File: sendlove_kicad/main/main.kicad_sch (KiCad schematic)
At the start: 0 parts

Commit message: feat(hw): schematic khoi nguon (USB-C, ESD, sac TP4056 + NTC, power-path, LDO)
- USB-C 16P, CC1/CC2 moi chan 5.1k rieng xuong GND, USBLC6-2SC6 tren D+/D-.
- TP4056: PROG 2k (~580mA), TEMP = NTC 10k B3950 + 6.2k tu VBUS (cua so sac
  ~5-45 do C, tinh theo nguong 45%/80% VCC; can doi chieu datasheet TP4056-42),
  CHRG -> LED do + 1k, STDBY bo trong.
- Power-path: VBUS -> SS14 -> VPATH; VBAT -> AO3401A (D=VBAT, S=VPATH,
  G=VBUS, 100k keo G xuong GND). Cong tac truot VPATH -> VSYS (sac van chay
  khi tat may).
- RT9080-33 (EN noi VSYS), 10uF vao/ra.
Them so voi BOM.md: NTC + 6.2k, 100k keo cong P-MOS, 10uF VBUS/VBAT.
Toan bo net noi bang nhan cuc bo; PWR_FLAG cho GND/VBUS/VSYS. ERC 0 loi.

Co-Authored-By: Claude Opus 5.5 <noreply@anthropic.com>
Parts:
- added C1, C2, C3, C4: 10uF, Capacitor_SMD:C_0805_2012Metric, symbol Device:C
- added D1: SS14, Diode_SMD:D_SMA, symbol Device:D_Schottky
- added D2: LED_Red, LED_SMD:LED_0603_1608Metric, symbol Device:LED
- added J1: USB-C 16P, Connector_USB:USB_C_Receptacle_HRO_TYPE-C-31-M-12, symbol Connector:USB_C_Receptacle_USB2.0_16P
- added J2: BATT, Connector_JST:JST_PH_S2B-PH-SM4-TB_1x02-1MP_P2.00mm_Horizontal, symbol Connector_Generic:Conn_01x02
- added Q1: AO3401A, Package_TO_SOT_SMD:SOT-23, symbol Transistor_FET:AO3401A
- added R1, R2: 5.1k, Resistor_SMD:R_0603_1608Metric, symbol Device:R
- added R3: 2k, Resistor_SMD:R_0603_1608Metric, symbol Device:R
- added R4: 6.2k 1%, Resistor_SMD:R_0603_1608Metric, symbol Device:R
- added R5: 1k, Resistor_SMD:R_0603_1608Metric, symbol Device:R
- added R6: 100k, Resistor_SMD:R_0603_1608Metric, symbol Device:R
- added SW1: POWER, Button_Switch_SMD:SW_SPDT_PCM12, symbol Switch:SW_SPDT
- added TH1: 10k B3950, Resistor_SMD:R_0603_1608Metric, symbol Device:Thermistor_NTC
- added U1: USBLC6-2SC6, Package_TO_SOT_SMD:SOT-23-6, symbol Power_Protection:USBLC6-2SC6
- added U2: TP4056-42-ESOP8, Package_SO:SOIC-8-1EP_3.9x4.9mm_P1.27mm_EP2.41x3.3mm_ThermalVias, symbol Battery_Management:TP4056-42-ESOP8
- added U3: RT9080-33GJ5, Package_TO_SOT_SMD:SOT-23-5, symbol SendLove:RT9080-33GJ5
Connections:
- new net +3V3: C4.1, U3.5 (VOUT)
- new net BAT_NTC: R4.2, TH1.1, U2.1 (TEMP)
- new net CC1: J1.A5 (CC1), R1.1
- new net CC2: J1.B5 (CC2), R2.1
- new net CHG_LED_K: D2.1 (K), R5.1
- new net CHG_PROG: R3.1, U2.2 (PROG)
- new net CHG_STAT: R5.2, U2.7 (~{CHRG})
- new net GND: C1.2, C2.2, C3.2, C4.2, J1.A1 (GND), J1.A12 (GND), J1.B1 (GND), J1.B12 (GND), J1.SH (SHIELD), J2.2 (Pin_2), R1.2, R2.2, R3.2, R6.2, TH1.2, U1.2 (GND), U2.3 (GND), U2.9 (EPAD), U3.2 (GND)
- new net USB_DN: J1.A7 (D-), J1.B7 (D-), U1.1 (I/O1), U1.6 (I/O1)
- new net USB_DP: J1.A6 (D+), J1.B6 (D+), U1.3 (I/O2), U1.4 (I/O2)
- new net VBAT: C2.1, J2.1 (Pin_1), Q1.3 (D), U2.5 (BAT)
- new net VBUS: C1.1, D1.2 (A), D2.2 (A), J1.A4 (VBUS), J1.A9 (VBUS), J1.B4 (VBUS), J1.B9 (VBUS), Q1.1 (G), R4.1, R6.1, U1.5 (VBUS), U2.4 (V_{CC}), U2.8 (CE)
- new net VPATH: D1.1 (K), Q1.2 (S), SW1.2 (B)
- new net VSYS: C3.1, SW1.1 (A), U3.1 (VIN), U3.3 (EN)
- no-connect marks 0 -> 4

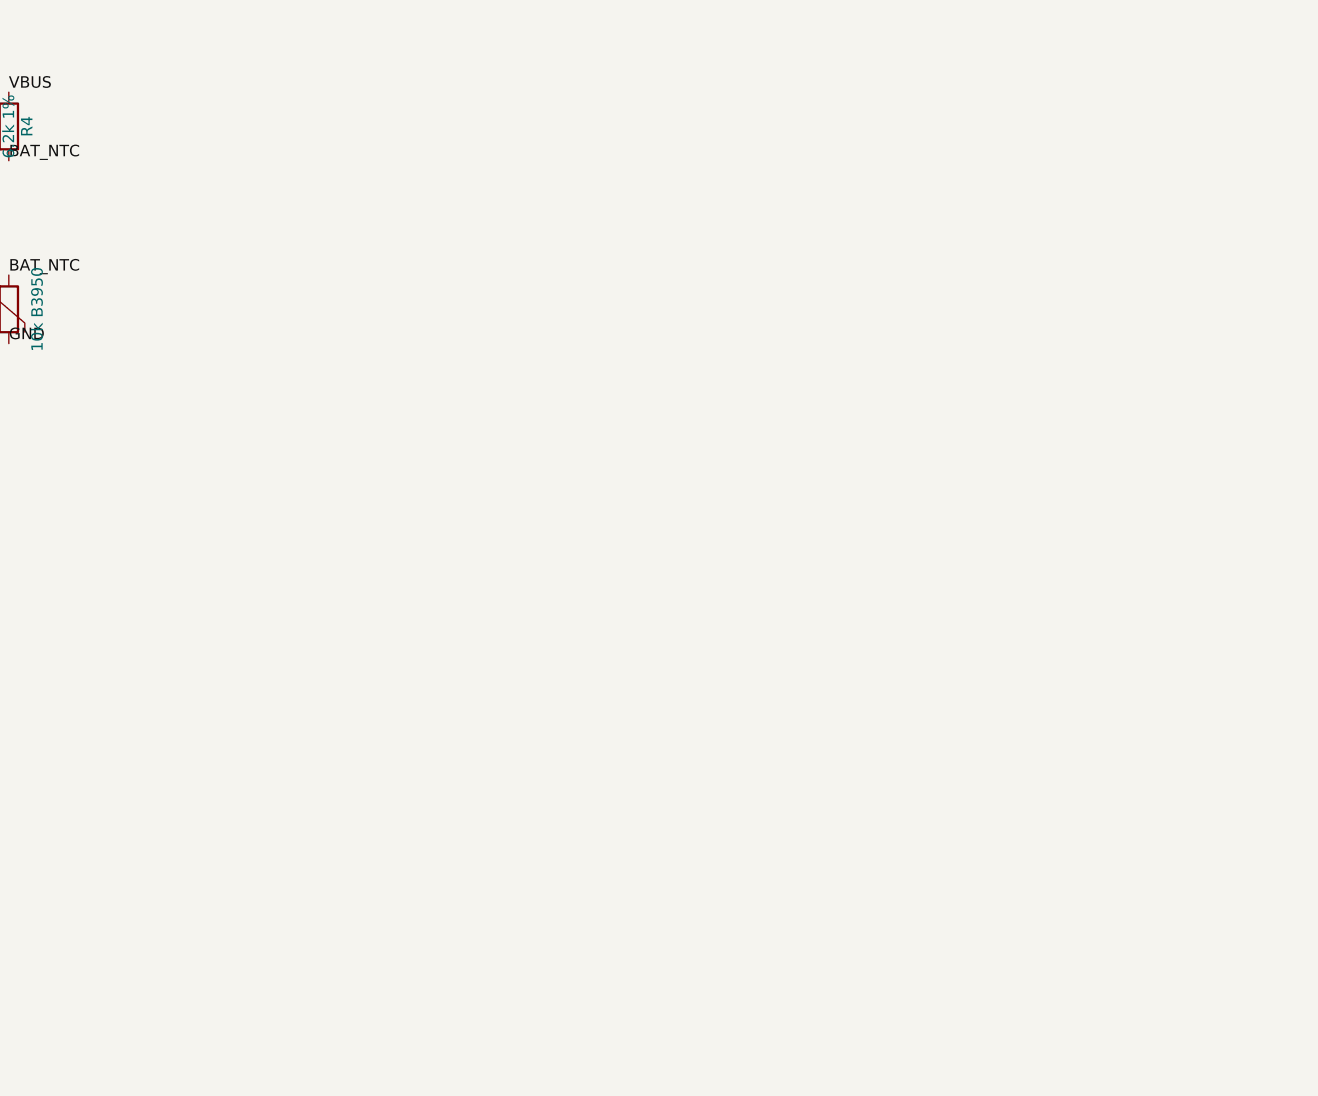
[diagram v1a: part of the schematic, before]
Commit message: feat(hw): schematic khoi vi dieu khien ESP32-C3-MINI-1
- 3V3: 10uF 0603 + 100nF 0402 sat chan. EN: 10k len 3V3 + 1uF xuong GND,
  nut RESET keo EN xuong GND.
- Strapping: 10k keo len o GPIO2 (I2S_DOUT), GPIO8 (SD_CS), GPIO9 (TFT_RST).
  Nut BOOT noi GPIO9 qua 1k (GPIO9 dang xuat HIGH cho TFT RST).
- Nhan net theo chuc nang dung bang chan BOM.md: I2S_BCLK/LRC/DOUT (0/1/2),
  TFT_BLK (3), SPI_SCK/MISO/MOSI (4/5/6), TFT_DC (7), SD_CS (8), TFT_RST (9),
  TOUCH_OUT (10), USB_DN/DP (18/19), AMP_EN (20), LED_NOTIFY (21).
Cac nhan ngoai vi chua co dau kia; se noi o cac khoi sau.

Co-Authored-By: Claude Opus 5.5 <noreply@anthropic.com>
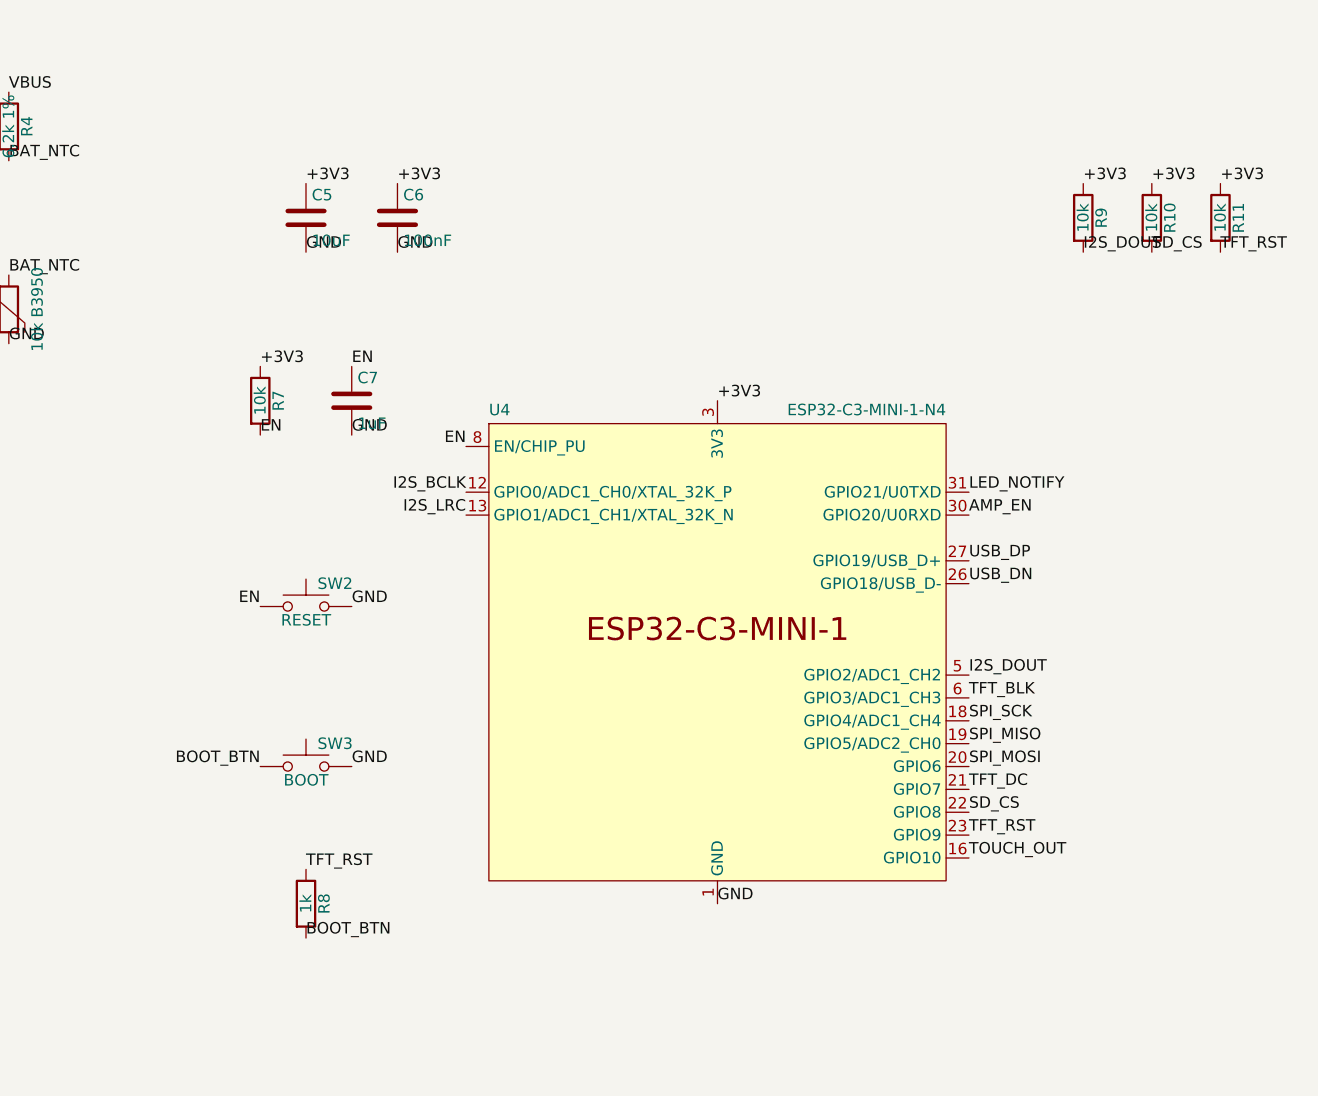
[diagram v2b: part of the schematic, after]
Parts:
- added C5: 10uF, Capacitor_SMD:C_0603_1608Metric, symbol Device:C
- added C6: 100nF, Capacitor_SMD:C_0402_1005Metric, symbol Device:C
- added C7: 1uF, Capacitor_SMD:C_0603_1608Metric, symbol Device:C
- added R10, R11, R7, R9: 10k, Resistor_SMD:R_0603_1608Metric, symbol Device:R
- added R8: 1k, Resistor_SMD:R_0603_1608Metric, symbol Device:R
- added SW2: RESET, Button_Switch_SMD:SW_SPST_PTS810, symbol Switch:SW_Push
- added SW3: BOOT, Button_Switch_SMD:SW_SPST_PTS810, symbol Switch:SW_Push
- added U4: ESP32-C3-MINI-1-N4, PCM_Espressif:ESP32-C3-MINI-1, symbol Espressif:ESP32-C3-MINI-1
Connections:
- net +3V3: now also C5.1, C6.1, R10.1, R11.1, R7.1, R9.1, U4.3 (3V3)
- net GND: now also C5.2, C6.2, C7.2, SW2.2, SW3.2, U4.1 (GND), U4.11 (GND), U4.14 (GND), U4.2 (GND), U4.36 (GND), U4.37 (GND), U4.38 (GND), U4.39 (GND), U4.40 (GND), U4.41 (GND), U4.42 (GND), U4.43 (GND), U4.44 (GND), U4.45 (GND), U4.46 (GND), U4.47 (GND), U4.48 (GND), U4.49 (GND), U4.50 (GND), U4.51 (GND), U4.52 (GND), U4.53 (GND)
- net USB_DN: now also U4.26 (GPIO18/USB_D-)
- net USB_DP: now also U4.27 (GPIO19/USB_D+)
- new net AMP_EN: U4.30 (GPIO20/U0RXD)
- new net BOOT_BTN: R8.2, SW3.1
- new net EN: C7.1, R7.2, SW2.1, U4.8 (EN/CHIP_PU)
- new net I2S_BCLK: U4.12 (GPIO0/ADC1_CH0/XTAL_32K_P)
- new net I2S_DOUT: R9.2, U4.5 (GPIO2/ADC1_CH2)
- new net I2S_LRC: U4.13 (GPIO1/ADC1_CH1/XTAL_32K_N)
- new net LED_NOTIFY: U4.31 (GPIO21/U0TXD)
- new net SD_CS: R10.2, U4.22 (GPIO8)
- new net SPI_MISO: U4.19 (GPIO5/ADC2_CH0)
- new net SPI_MOSI: U4.20 (GPIO6)
- new net SPI_SCK: U4.18 (GPIO4/ADC1_CH4)
- new net TFT_BLK: U4.6 (GPIO3/ADC1_CH3)
- new net TFT_DC: U4.21 (GPIO7)
- new net TFT_RST: R11.2, R8.1, U4.23 (GPIO9)
- new net TOUCH_OUT: U4.16 (GPIO10)

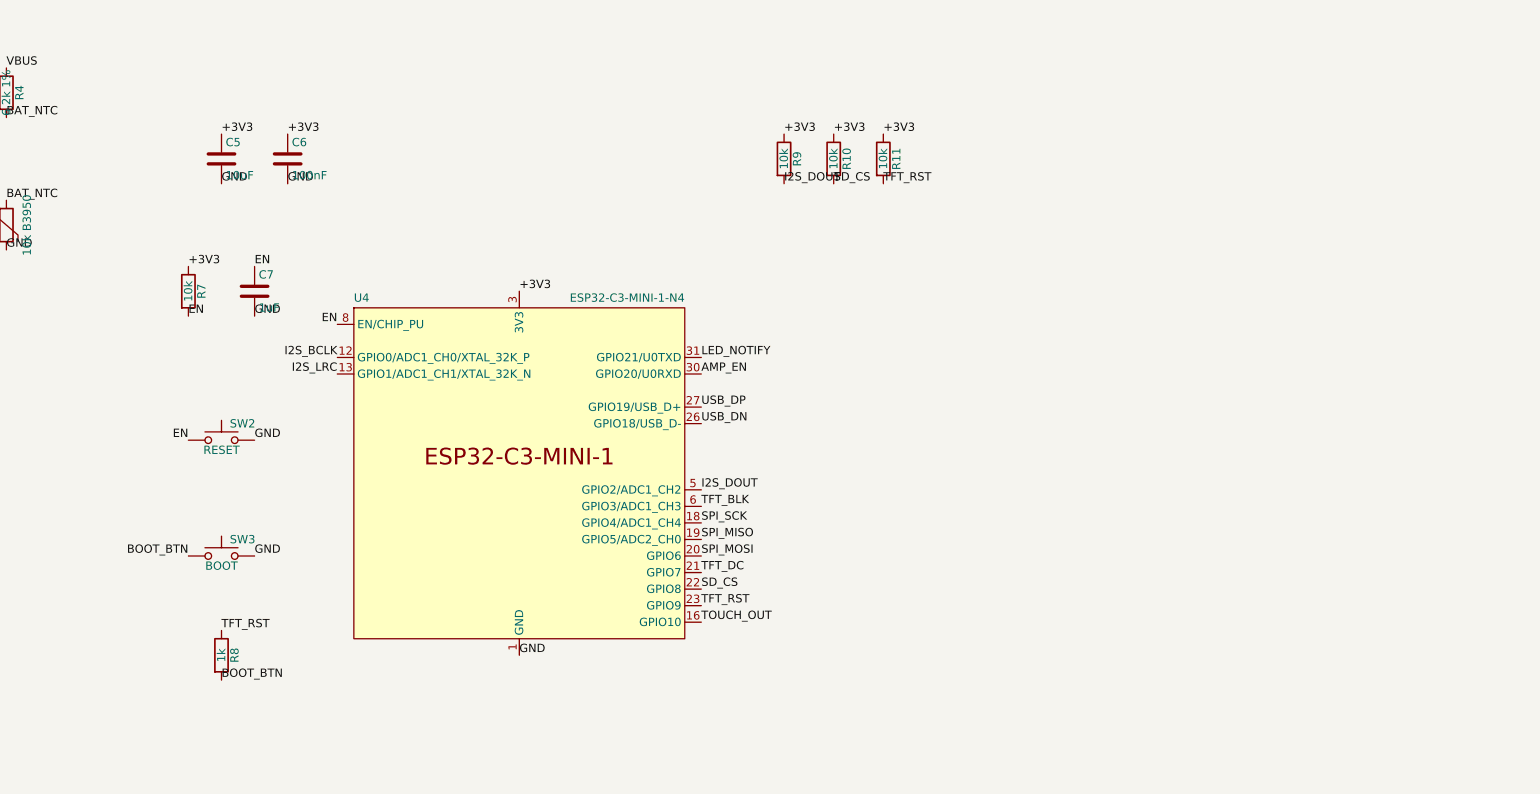
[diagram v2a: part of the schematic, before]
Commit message: feat(hw): schematic khoi man hinh + microSD
- J3 header 1x7 cho module LCD ST7789 (GND VCC SCL SDA RES DC BLK). BLK noi
  thang GPIO3: dung module co san mach den nen nen bo MOSFET (BOM.md ghi chi
  can khi dung panel tran).
- J4 khe microSD Hirose DM3AT, che do SPI: CS=SD_CS, CMD=SPI_MOSI,
  CLK=SPI_SCK, DAT0=SPI_MISO. 10k keo len CMD, DAT0, DAT1, DAT2 (CS da co
  R10 o khoi MCU). 10uF + 100nF nguon the. DET_A/DET_B bo trong (het GPIO).
SPI_SCK/SPI_MOSI dung chung man hinh + the nhu firmware.

Co-Authored-By: Claude Opus 5.5 <noreply@anthropic.com>
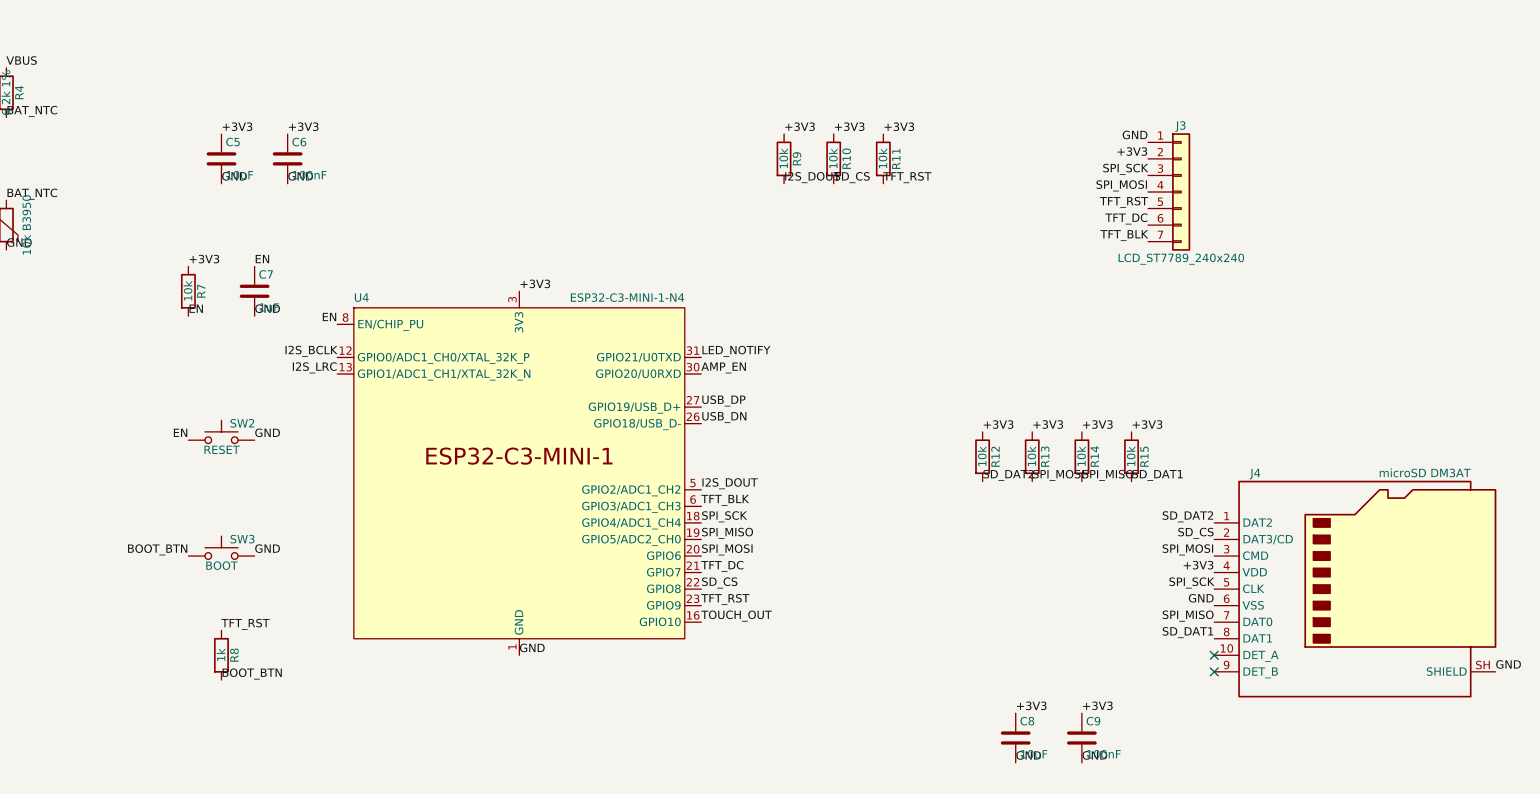
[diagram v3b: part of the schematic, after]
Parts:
- added C8: 10uF, Capacitor_SMD:C_0603_1608Metric, symbol Device:C
- added C9: 100nF, Capacitor_SMD:C_0402_1005Metric, symbol Device:C
- added J3: LCD_ST7789_240x240, Connector_PinHeader_2.54mm:PinHeader_1x07_P2.54mm_Vertical, symbol Connector_Generic:Conn_01x07
- added J4: microSD DM3AT, Connector_Card:microSD_HC_Hirose_DM3AT-SF-PEJM5, symbol Connector:Micro_SD_Card_Det_Hirose_DM3AT
- added R12, R13, R14, R15: 10k, Resistor_SMD:R_0603_1608Metric, symbol Device:R
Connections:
- net +3V3: now also C8.1, C9.1, J3.2 (Pin_2), J4.4 (VDD), R12.1, R13.1, R14.1, R15.1
- net GND: now also C8.2, C9.2, J3.1 (Pin_1), J4.6 (VSS), J4.SH (SHIELD)
- net SD_CS: now also J4.2 (DAT3/CD)
- net SPI_MISO: now also J4.7 (DAT0), R14.2
- net SPI_MOSI: now also J3.4 (Pin_4), J4.3 (CMD), R13.2
- net SPI_SCK: now also J3.3 (Pin_3), J4.5 (CLK)
- net TFT_BLK: now also J3.7 (Pin_7)
- net TFT_DC: now also J3.6 (Pin_6)
- net TFT_RST: now also J3.5 (Pin_5)
- new net SD_DAT1: J4.8 (DAT1), R15.2
- new net SD_DAT2: J4.1 (DAT2), R12.2
- no-connect marks 4 -> 6

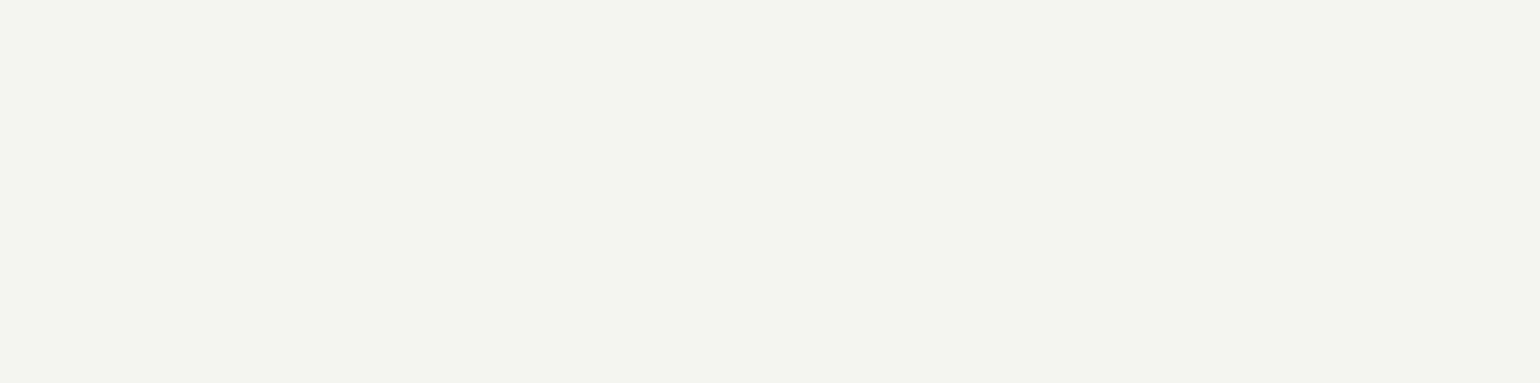
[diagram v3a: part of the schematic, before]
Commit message: feat(hw): schematic khoi am thanh, cam ung, LED thong bao
- MAX98357A: VDD = VSYS (khong qua LDO), 10uF + 100nF; DIN/BCLK/LRCLK =
  I2S_DOUT/BCLK/LRC; SD_MODE qua 680k tu AMP_EN (GPIO20); GAIN_SLOT de ho
  (9dB); EP noi GND. Loa qua JST-PH 2 chan.
- TTP223-BA6: AHLB = GND (active HIGH), TOG = GND (direct), Cs 10pF (chinh
  0-50pF khi co vo that), 100nF nguon; Q -> TOUCH_OUT (GPIO10). Pad cam ung
  tam dung footprint 4mm, ve pad that o buoc PCB.
- LED thong bao: GPIO21 -> 1k -> LED -> GND.
Toan bo schematic: ERC 0 loi, 1 canh bao (EP cua MAX98357A la chan
"Unspecified" noi GND, dung theo datasheet); khong net nao chi mot chan.

Co-Authored-By: Claude Opus 5.5 <noreply@anthropic.com>
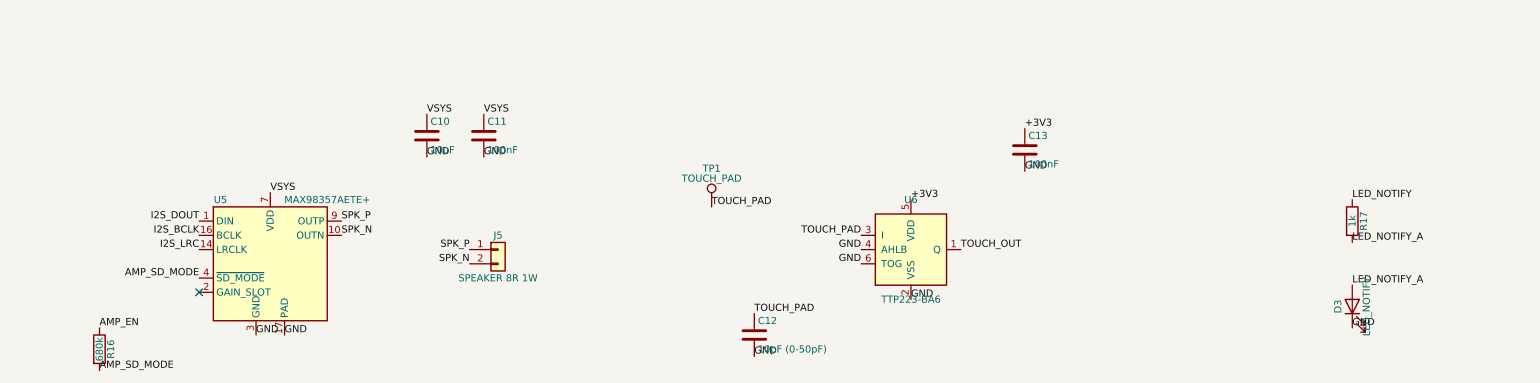
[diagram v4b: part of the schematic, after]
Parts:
- added C10: 10uF, Capacitor_SMD:C_0805_2012Metric, symbol Device:C
- added C11, C13: 100nF, Capacitor_SMD:C_0402_1005Metric, symbol Device:C
- added C12: 10pF (0-50pF), Capacitor_SMD:C_0603_1608Metric, symbol Device:C
- added D3: LED_NOTIFY, LED_SMD:LED_0603_1608Metric, symbol Device:LED
- added J5: SPEAKER 8R 1W, Connector_JST:JST_PH_S2B-PH-SM4-TB_1x02-1MP_P2.00mm_Horizontal, symbol Connector_Generic:Conn_01x02
- added R16: 680k, Resistor_SMD:R_0603_1608Metric, symbol Device:R
- added R17: 1k, Resistor_SMD:R_0603_1608Metric, symbol Device:R
- added TP1: TOUCH_PAD, TestPoint:TestPoint_Pad_D4.0mm, symbol Connector:TestPoint
- added U5: MAX98357AETE+, Package_DFN_QFN:TQFN-16-1EP_3x3mm_P0.5mm_EP1.23x1.23mm, symbol Audio:MAX98357A
- added U6: TTP223-BA6, Package_TO_SOT_SMD:SOT-23-6, symbol SendLove:TTP223-BA6
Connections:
- net +3V3: now also C13.1, U6.5 (VDD)
- net AMP_EN: now also R16.1
- net GND: now also C10.2, C11.2, C12.2, C13.2, D3.1 (K), U5.11 (GND), U5.15 (GND), U5.17 (PAD), U5.3 (GND), U6.2 (VSS), U6.4 (AHLB), U6.6 (TOG)
- net I2S_BCLK: now also U5.16 (BCLK)
- net I2S_DOUT: now also U5.1 (DIN)
- net I2S_LRC: now also U5.14 (LRCLK)
- net LED_NOTIFY: now also R17.1
- net TOUCH_OUT: now also U6.1 (Q)
- net VSYS: now also C10.1, C11.1, U5.7 (VDD), U5.8 (VDD)
- new net AMP_SD_MODE: R16.2, U5.4 (~{SD_MODE})
- new net LED_NOTIFY_A: D3.2 (A), R17.2
- new net SPK_N: J5.2 (Pin_2), U5.10 (OUTN)
- new net SPK_P: J5.1 (Pin_1), U5.9 (OUTP)
- new net TOUCH_PAD: C12.1, TP1.1, U6.3 (I)
- no-connect marks 6 -> 7
